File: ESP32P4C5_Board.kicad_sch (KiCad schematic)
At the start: 0 parts

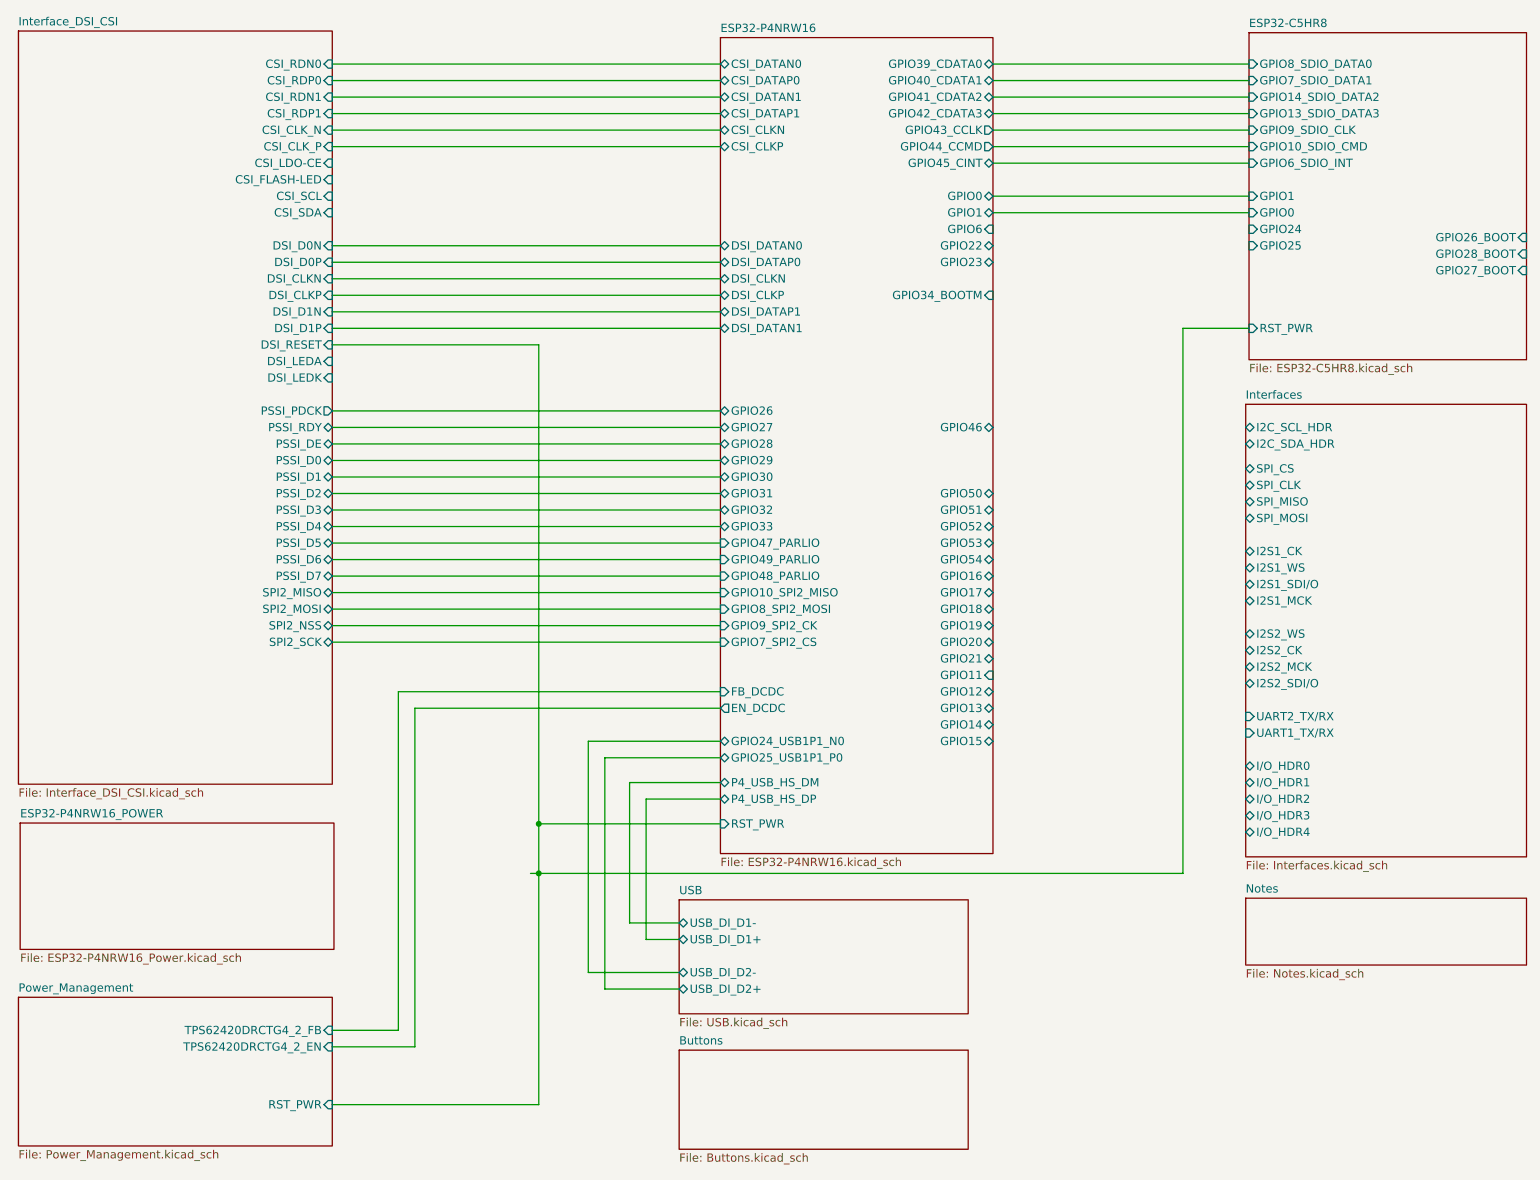
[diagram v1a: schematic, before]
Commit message: QSPI Memory Bus
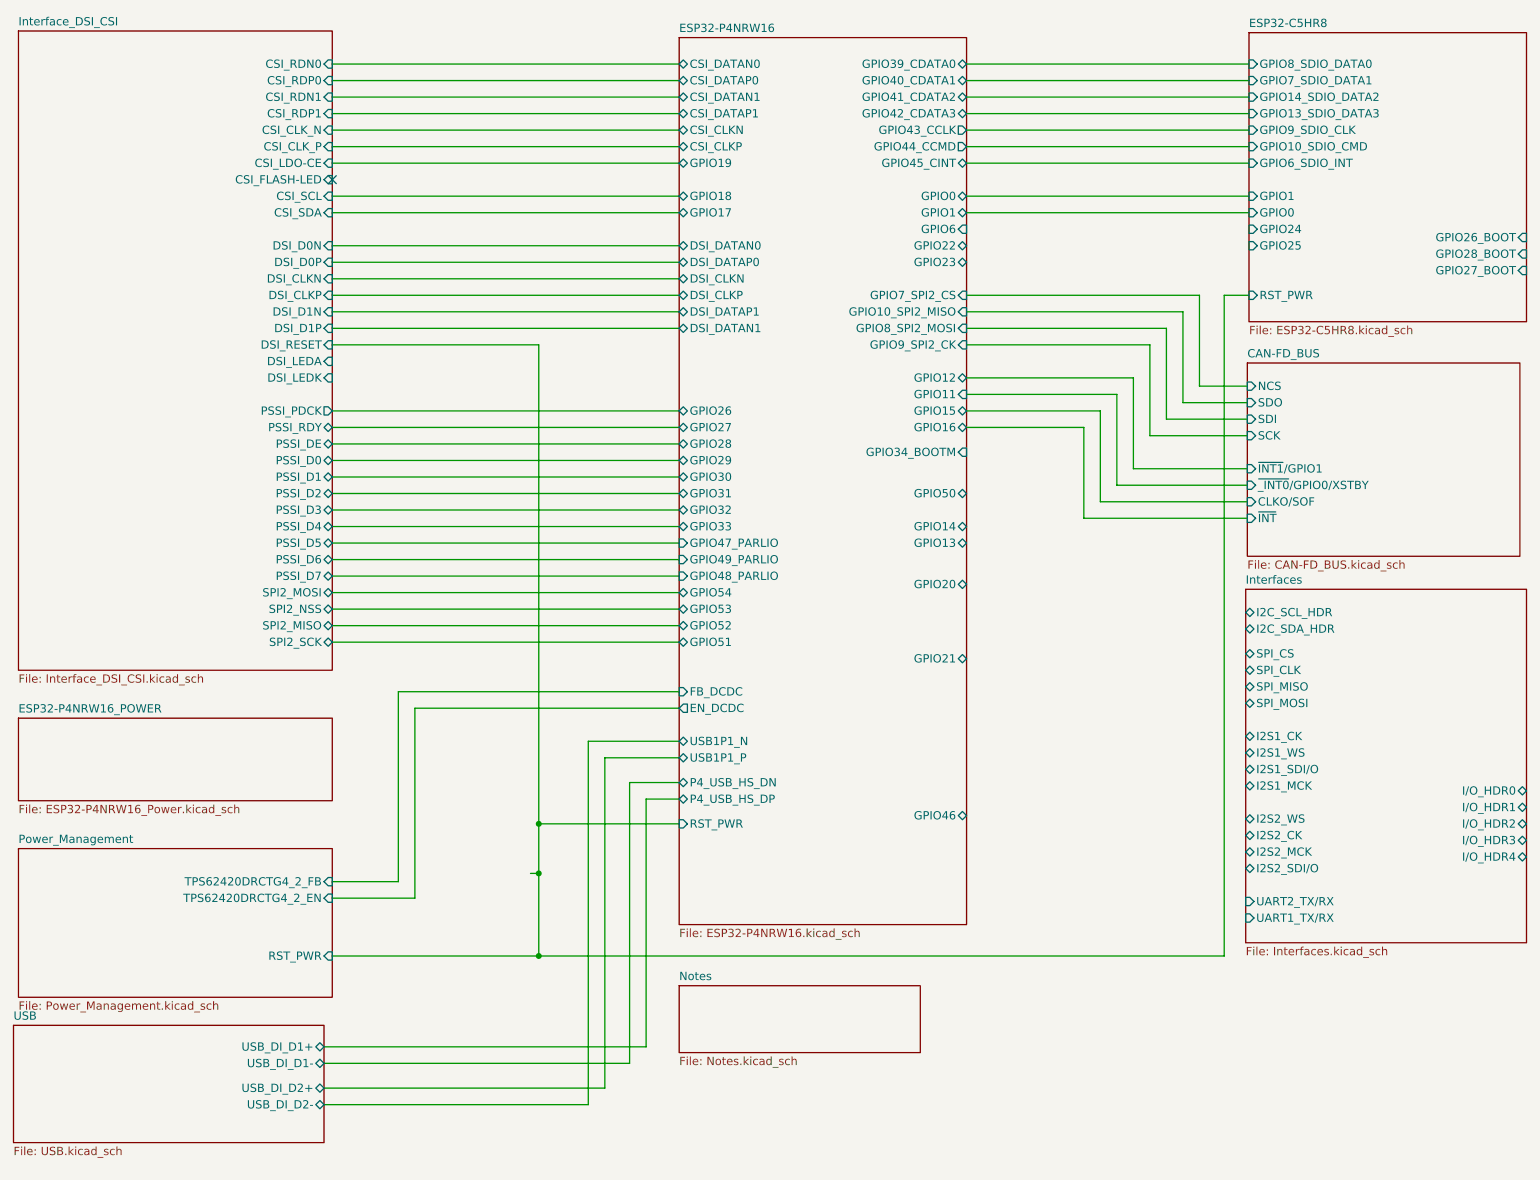
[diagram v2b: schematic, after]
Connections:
- no-connect marks 0 -> 1
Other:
- removed sheet Buttons
- added sheet CAN-FD_BUS (CAN-FD_BUS.kicad_sch)
- sheet ESP32-P4NRW16 ports: added P4_USB_HS_DN, USB1P1_N, USB1P1_P; removed GPIO24_USB1P1_N0, GPIO25_USB1P1_P0, P4_USB_HS_DM

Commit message: Interface Update
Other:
- sheet ESP32-C5HR8 ports: added none; removed GPIO26_BOOT, GPIO27_BOOT, GPIO28_BOOT
- sheet ESP32-P4NRW16 ports: added GPIO20_SPI_MOSI, GPIO21_SPI_MISO, GPIO22_SPI_CLK, GPIO23_SPI_CS, GPIO37_BOOTM_UART0_TXD, GPIO38_BOOTM_UART0_RXD; removed GPIO13, GPIO16, GPIO20, GPIO21, GPIO22, GPIO23, GPIO34_BOOTM
- sheet Interfaces ports: added UART0_RXD, UART0_TXD; removed I2S1_CK, I2S1_MCK, I2S1_SDI/O, I2S1_WS, I2S2_CK, I2S2_MCK, I2S2_SDI/O, I2S2_WS, I/O_HDR0, I/O_HDR1, I/O_HDR2, I/O_HDR3, I/O_HDR4, UART1_TX/RX, UART2_TX/RX
- sheet Power_Management ports: added PG1_TPS62442RQRR, PG2_TPS62442RQRR, TPS62442RQRR_2_EN, TPS62442RQRR_2_FB; removed TPS62420DRCTG4_2_EN, TPS62420DRCTG4_2_FB
- company: (none) -> Peter Hancak
- title: (none) -> ESP32P4C5_BOARD

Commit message: Power rail update
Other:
- sheet Interfaces ports: added SPI_0_CLK_R, SPI_0_CS_R, SPI_0_MISO_R, SPI_0_MOSI_R; removed SPI_CLK, SPI_CS, SPI_MISO, SPI_MOSI
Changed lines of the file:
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@@
-			)
-		)
-		(pin "SPI_CS" bidirectional
-			(at 220.98 124.46 180)
-			(effects
-				(font
-					(size 1.27 1.27)
-				)
-				(justify left)
-			)
-		)
-		(pin "SPI_CLK" bidirectional
-			(at 220.98 127 180)
-			(effects
-				(font
-					(size 1.27 1.27)
-				)
-				(justify left)
-			)
-		)
-		(pin "SPI_MISO" bidirectional
-			(at 220.98 129.54 180)
-			(effects
-				(font
-					(size 1.27 1.27)
-				)
-				(justify left)
-			)
-		)
-		(pin "SPI_MOSI" bidirectional
-			(at 220.98 132.08 180)
-			(effects
-				(font
-					(size 1.27 1.27)
-				)
-				(justify left)
 			)
 		)
@@
 			(effects
 				(font
+					(size 1.27 1.27)
+				)
+				(justify left)
+			)
+		)
+		(pin "SPI_0_CLK_R" bidirectional
+			(at 220.98 127 180)
+			(effects
+				(font
+					(size 1.27 1.27)
+				)
+				(justify left)
+			)
+		)
+		(pin "SPI_0_CS_R" bidirectional
+			(at 220.98 124.46 180)
+			(effects
+				(font
+					(size 1.27 1.27)
+				)
+				(justify left)
+			)
+		)
+		(pin "SPI_0_MISO_R" bidirectional
+			(at 220.98 129.54 180)
+			(effects
+				(font
+					(size 1.27 1.27)
+				)
+				(justify left)
+			)
+		)
+		(pin "SPI_0_MOSI_R" bidirectional
+			(at 220.98 132.08 180)
+			(effects
+				(font

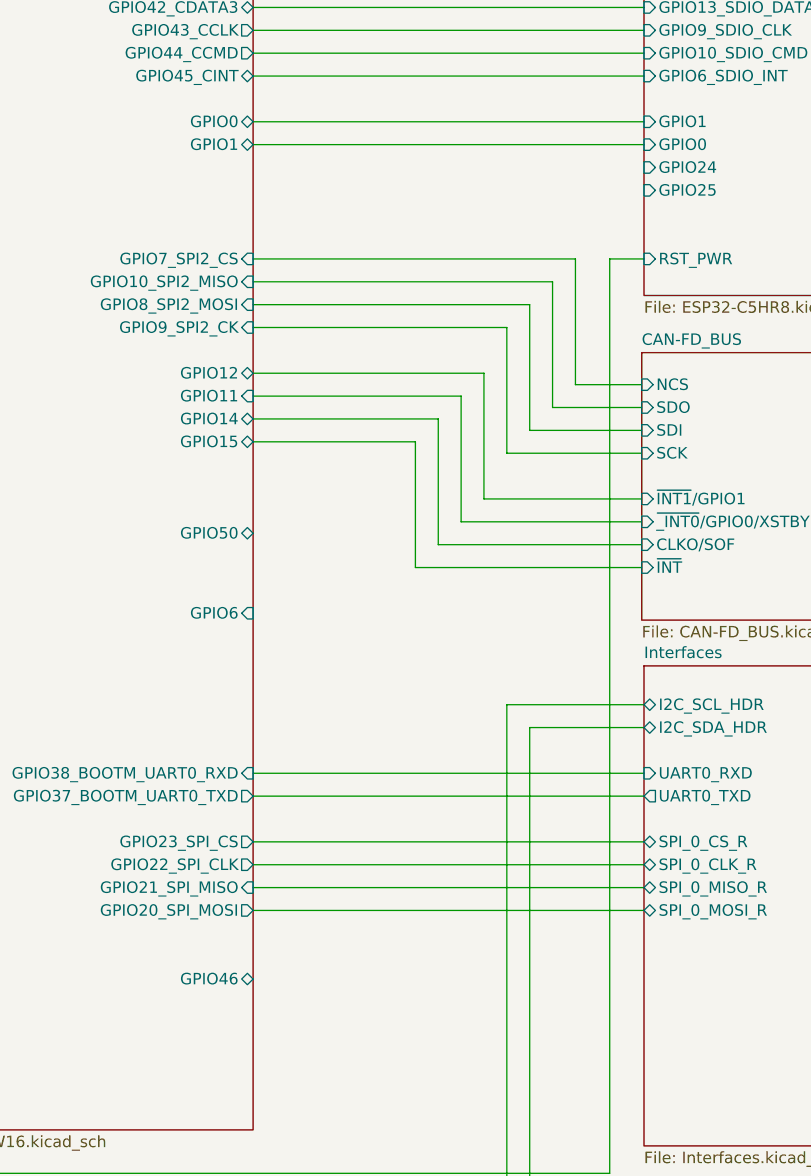
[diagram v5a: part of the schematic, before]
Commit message: Power Rail Update
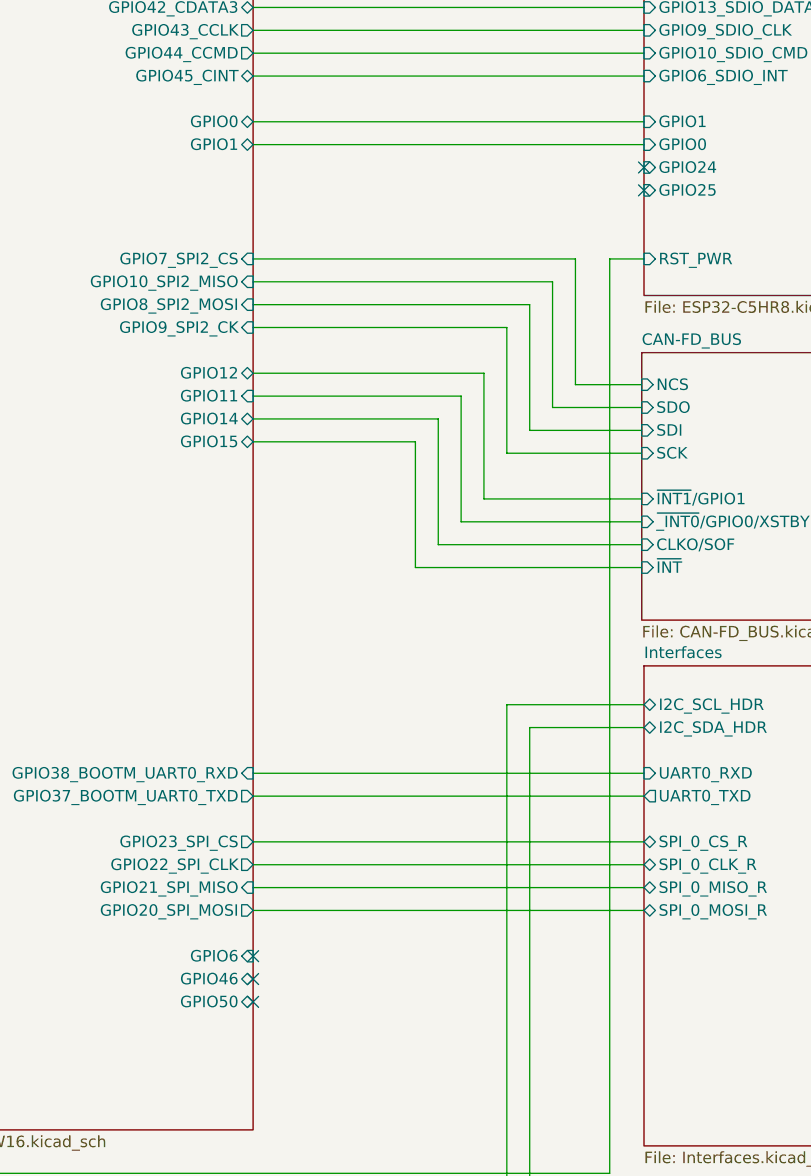
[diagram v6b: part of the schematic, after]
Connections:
- no-connect marks 1 -> 6
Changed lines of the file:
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@@
 		(at 80.01 41.91)
+	)
+	(no_connect
+		(at 177.546 139.7)
+	)
+	(no_connect
+		(at 177.546 142.24)
+	)
+	(no_connect
+		(at 220.98 52.07)
+	)
+	(no_connect
+		(at 220.98 49.53)
+	)
+	(no_connect
+		(at 177.546 137.16)
 	)
 	(wire
@@
 		)
 		(pin "GPIO50" bidirectional
-			(at 177.546 90.17 0)
+			(at 177.546 142.24 0)
 			(effects
 				(font
@@
 		)
 		(pin "GPIO6" input
-			(at 177.546 99.06 0)
-			(effects
-				(font
+			(at 177.546 137.16 0)
+			(effects
+				(font
